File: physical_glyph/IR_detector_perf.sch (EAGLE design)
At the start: 18 parts, among them IC1 7805T, T1 BP103, U1 MCP6004-I/P, U2 LM339PWR

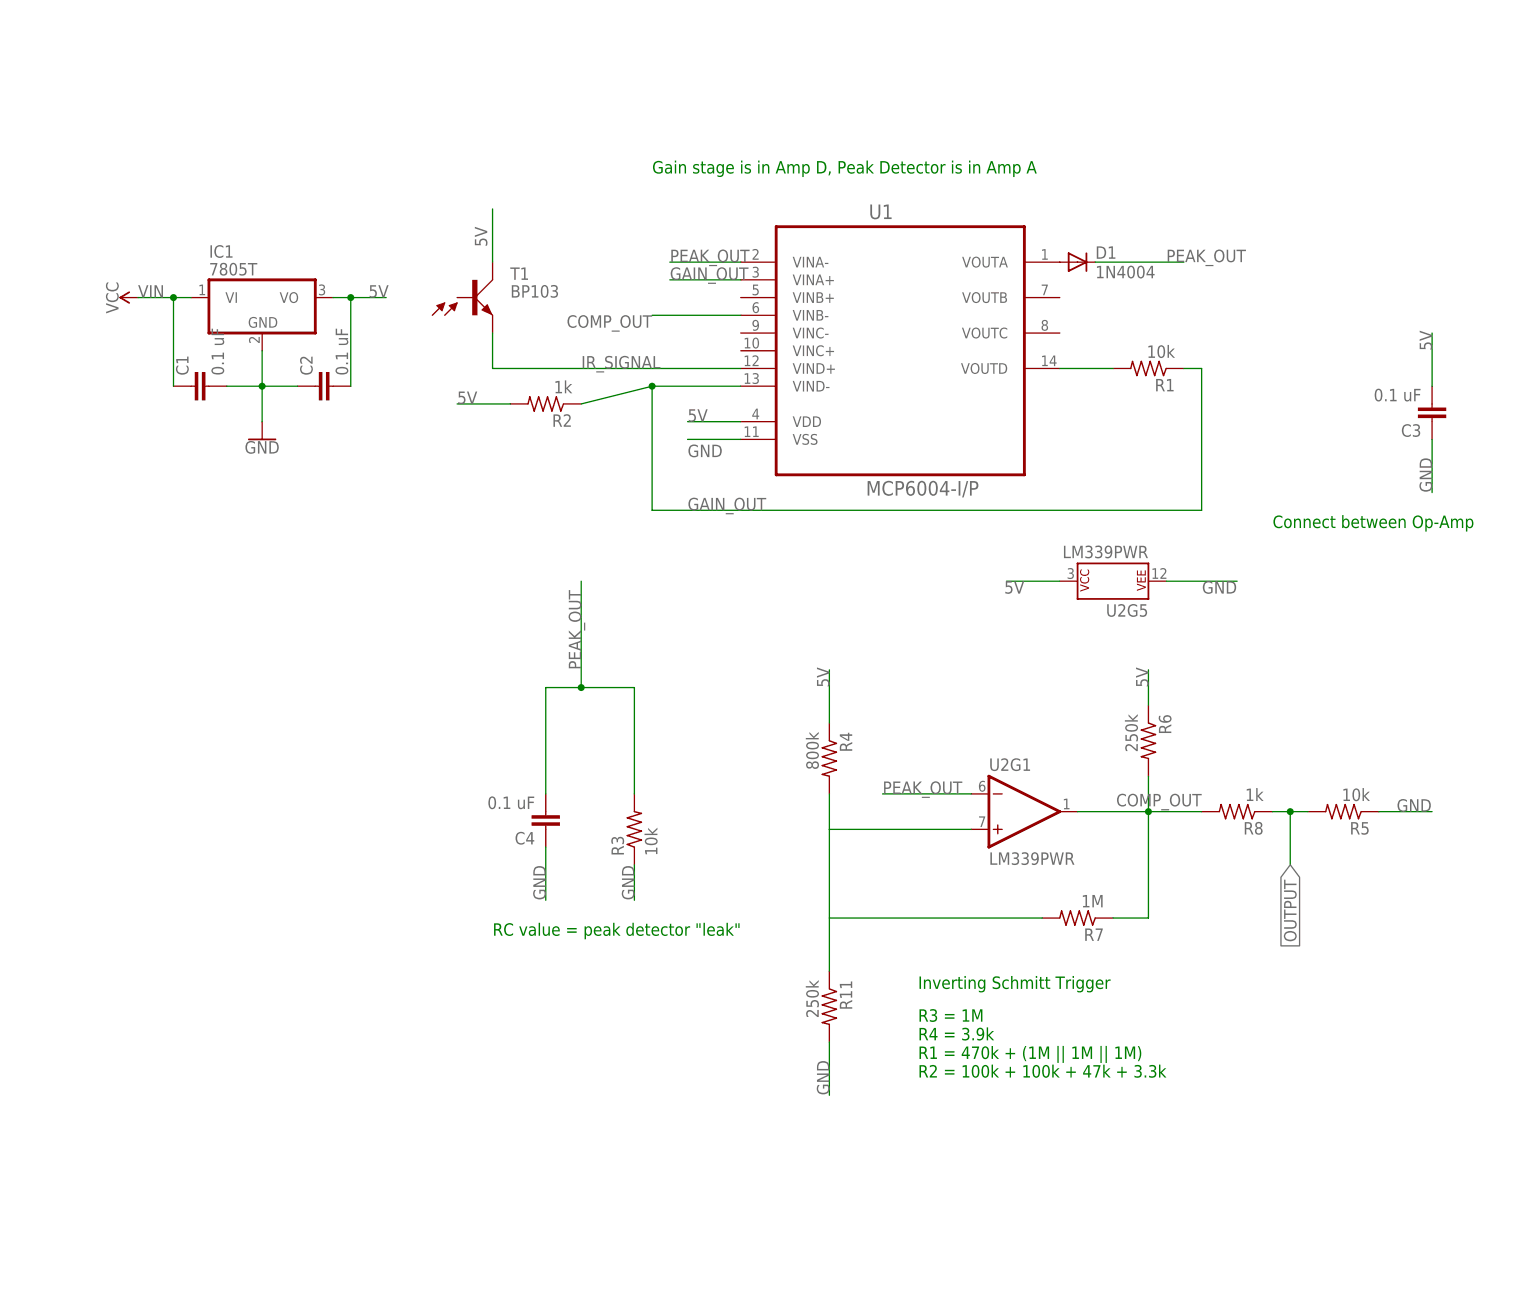
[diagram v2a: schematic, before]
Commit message: Change gain stage and output
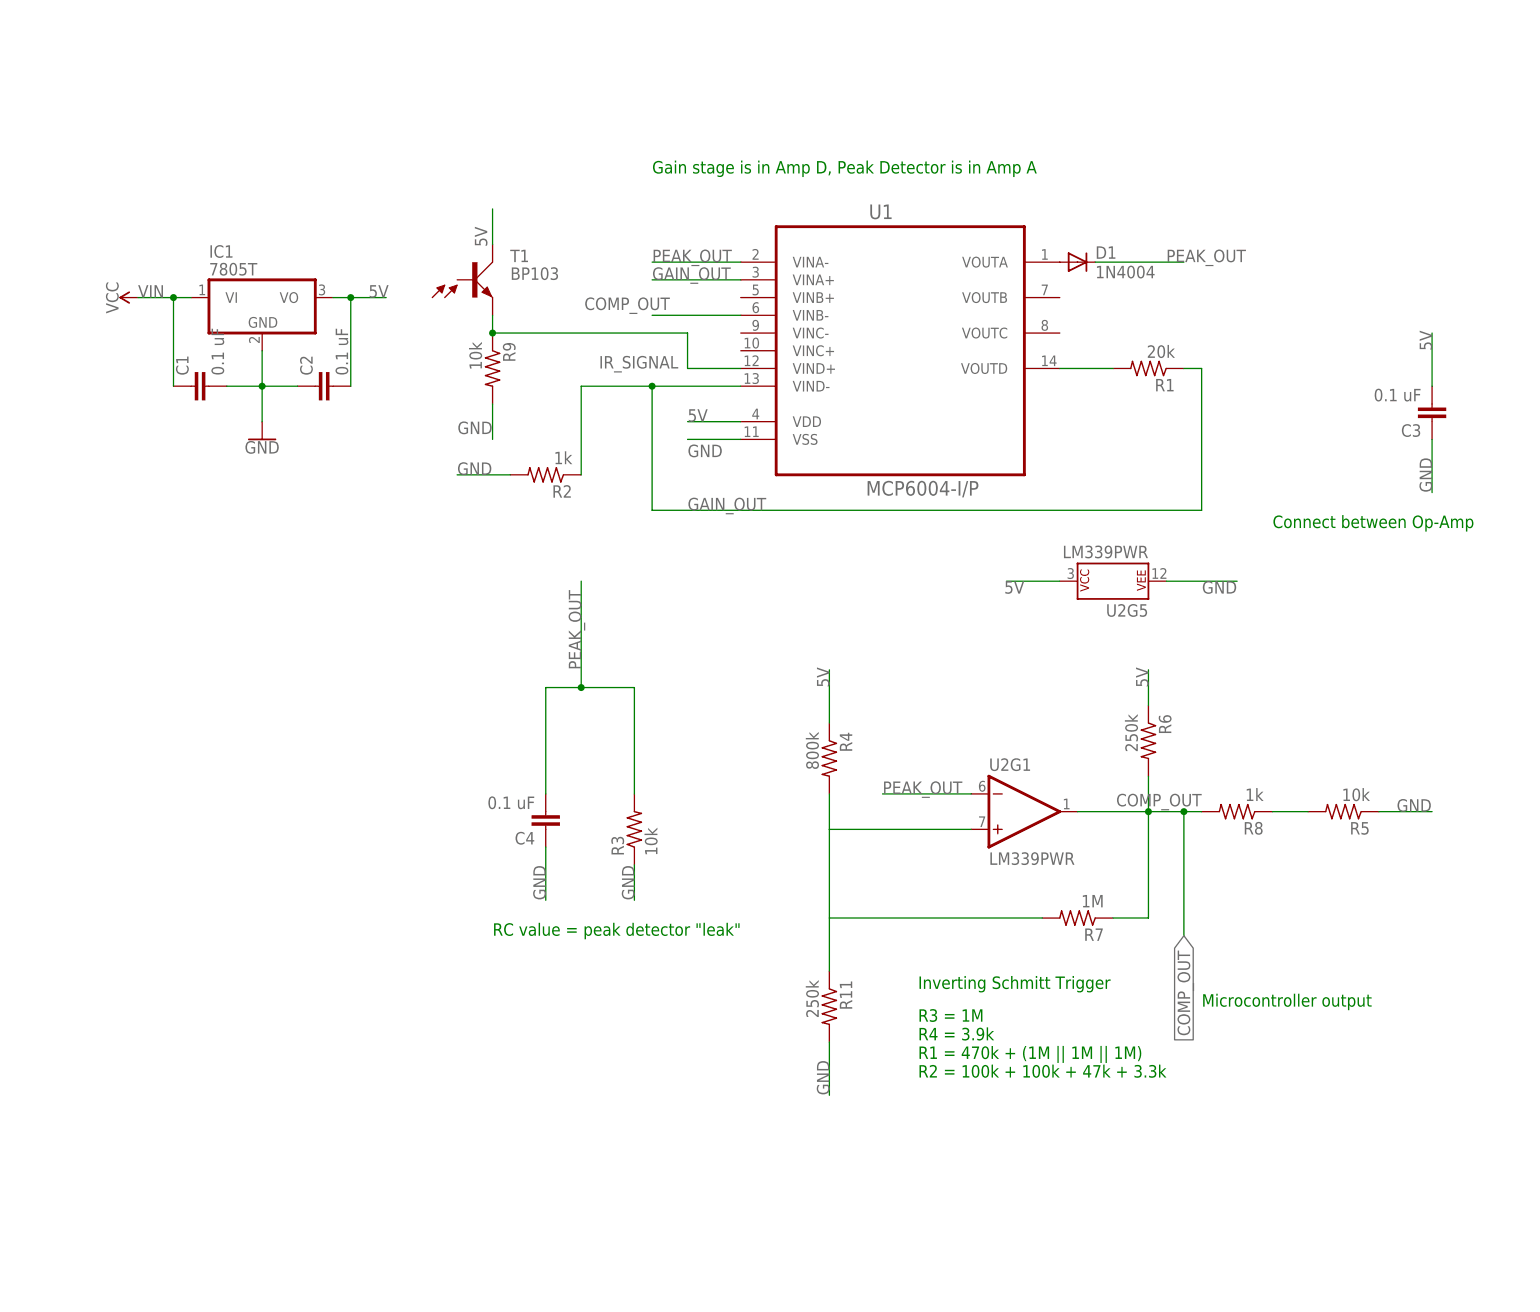
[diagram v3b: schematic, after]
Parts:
- added R9: 10k, rcl:R-US_0204/2V
- R1: value 10k -> 20k
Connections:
- net OUTPUT renamed N$1
- net 5V: no longer R2.2
- net GND: now also R2.2, R9.2
- net IR_SIGNAL: now also R9.1
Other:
- note added: "Microcontroller output"
- moved on the sheet: R2, T1
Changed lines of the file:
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@@
 <part name="C2" library="resistor" library_urn="urn:adsk.eagle:library:348" deviceset="C-EU" device="025-024X044" package3d_urn="urn:adsk.eagle:package:26149/1" value="0.1 uF"/>
 <part name="T1" library="opto-trans-siemens" library_urn="urn:adsk.eagle:library:317" deviceset="BP103" device="" package3d_urn="urn:adsk.eagle:package:21787/1"/>
-<part name="R1" library="rcl" library_urn="urn:adsk.eagle:library:334" deviceset="R-US_" device="0204/2V" package3d_urn="urn:adsk.eagle:package:23495/1" value="10k"/>
+<part name="R1" library="rcl" library_urn="urn:adsk.eagle:library:334" deviceset="R-US_" device="0204/2V" package3d_urn="urn:adsk.eagle:package:23495/1" value="20k"/>
 <part name="R2" library="rcl" library_urn="urn:adsk.eagle:library:334" deviceset="R-US_" device="0204/2V" package3d_urn="urn:adsk.eagle:package:23495/1" value="1k"/>
 <part name="R3" library="rcl" library_urn="urn:adsk.eagle:library:334" deviceset="R-US_" device="0204/2V" package3d_urn="urn:adsk.eagle:package:23495/1" value="10k"/>
@@
 <part name="R5" library="rcl" library_urn="urn:adsk.eagle:library:334" deviceset="R-US_" device="0204/2V" package3d_urn="urn:adsk.eagle:package:23495/1" value="10k"/>
 <part name="R8" library="rcl" library_urn="urn:adsk.eagle:library:334" deviceset="R-US_" device="0204/2V" package3d_urn="urn:adsk.eagle:package:23495/1" value="1k"/>
+<part name="R9" library="rcl" library_urn="urn:adsk.eagle:library:334" deviceset="R-US_" device="0204/2V" package3d_urn="urn:adsk.eagle:package:23495/1" value="10k"/>
 </parts>
 <sheets>
@@
 <text x="17.78" y="-7.62" size="1.778" layer="91">RC value = peak detector "leak"</text>
 <text x="78.74" y="-15.24" size="1.778" layer="91">Inverting Schmitt Trigger</text>
+<text x="119.38" y="-17.78" size="1.778" layer="91">Microcontroller output</text>
 </plain>
 <instances>
@@
 <instance part="C1" gate="G$1" x="-25.4" y="71.12" rot="R90"/>
 <instance part="C2" gate="G$1" x="-7.62" y="71.12" rot="R90"/>
-<instance part="T1" gate="1" x="15.24" y="83.82"/>
+<instance part="T1" gate="1" x="15.24" y="86.36"/>
 <instance part="R1" gate="G$1" x="111.76" y="73.66" rot="R180"/>
-<instance part="R2" gate="G$1" x="25.4" y="68.58" rot="R180"/>
+<instance part="R2" gate="G$1" x="25.4" y="58.42" rot="R180"/>
 <instance part="R3" gate="G$1" x="38.1" y="7.62" rot="R90"/>
 <instance part="R4" gate="G$1" x="66.04" y="17.78" rot="R270"/>
@@
 <instance part="R5" gate="G$1" x="139.7" y="10.16" rot="R180"/>
 <instance part="R8" gate="G$1" x="124.46" y="10.16" rot="R180"/>
+<instance part="R9" gate="G$1" x="17.78" y="73.66" rot="R270"/>
 </instances>
 <busses>
@@
 <segment>
 <pinref part="T1" gate="1" pin="C"/>
-<wire x1="17.78" y1="88.9" x2="17.78" y2="96.52" width="0.1524" layer="91"/>
+<wire x1="17.78" y1="91.44" x2="17.78" y2="96.52" width="0.1524" layer="91"/>
 <label x="15.24" y="93.98" size="1.778" layer="95" rot="R270"/>
-</segment>
-<segment>
-<pinref part="R2" gate="G$1" pin="2"/>
-<wire x1="20.32" y1="68.58" x2="12.7" y2="68.58" width="0.1524" layer="91"/>
-<label x="12.7" y="68.58" size="1.778" layer="95"/>
 </segment>
 <segment>
@@
 <label x="147.32" y="10.16" size="1.778" layer="95"/>
 </segment>
+<segment>
+<pinref part="R9" gate="G$1" pin="2"/>
+<wire x1="17.78" y1="68.58" x2="17.78" y2="63.5" width="0.1524" layer="91"/>
+<label x="17.78" y="66.04" size="1.778" layer="95" rot="R180"/>
+</segment>
+<segment>
+<pinref part="R2" gate="G$1" pin="2"/>
+<wire x1="20.32" y1="58.42" x2="12.7" y2="58.42" width="0.1524" layer="91"/>
+<label x="12.7" y="58.42" size="1.778" layer="95"/>
+</segment>
 </net>
 <net name="IR_SIGNAL" class="0">
 <segment>
 <pinref part="T1" gate="1" pin="E"/>
-<wire x1="17.78" y1="78.74" x2="17.78" y2="73.66" width="0.1524" layer="91"/>
+<wire x1="17.78" y1="81.28" x2="17.78" y2="78.74" width="0.1524" layer="91"/>
 <pinref part="U1" gate="A" pin="VIND+"/>
-<wire x1="17.78" y1="73.66" x2="53.34" y2="73.66" width="0.1524" layer="91"/>
-<label x="30.48" y="73.66" size="1.778" layer="95"/>
+<wire x1="17.78" y1="78.74" x2="45.72" y2="78.74" width="0.1524" layer="91"/>
+<wire x1="45.72" y1="78.74" x2="45.72" y2="73.66" width="0.1524" layer="91"/>
+<wire x1="45.72" y1="73.66" x2="53.34" y2="73.66" width="0.1524" layer="91"/>
+<label x="33.02" y="73.66" size="1.778" layer="95"/>
+<pinref part="R9" gate="G$1" pin="1"/>
+<junction x="17.78" y="78.74"/>
 </segment>
 </net>
@@
 <wire x1="40.64" y1="53.34" x2="40.64" y2="71.12" width="0.1524" layer="91"/>
 <pinref part="R2" gate="G$1" pin="1"/>
-<wire x1="30.48" y1="68.58" x2="40.64" y2="71.12" width="0.1524" layer="91"/>
+<wire x1="30.48" y1="58.42" x2="30.48" y2="71.12" width="0.1524" layer="91"/>
+<wire x1="30.48" y1="71.12" x2="40.64" y2="71.12" width="0.1524" layer="91"/>
 <junction x="40.64" y="71.12"/>
 <label x="45.72" y="53.34" size="1.778" layer="95"/>
@@
 <segment>
 <pinref part="U1" gate="A" pin="VINA+"/>
-<wire x1="53.34" y1="86.36" x2="43.18" y2="86.36" width="0.1524" layer="91"/>
-<label x="43.18" y="86.36" size="1.778" layer="95"/>
+<wire x1="53.34" y1="86.36" x2="40.64" y2="86.36" width="0.1524" layer="91"/>
+<label x="40.64" y="86.36" size="1.778" layer="95"/>
 </segment>
 </net>
@@
 <pinref part="U1" gate="A" pin="VINB-"/>
 <wire x1="53.34" y1="81.28" x2="40.64" y2="81.28" width="0.1524" layer="91"/>
-<label x="40.64" y="81.28" size="1.778" layer="95" rot="R180"/>
-</segment>
-<segment>
+<label x="43.18" y="83.82" size="1.778" layer="95" rot="R180"/>
+</segment>
+<segment>
+<label x="116.84" y="-7.62" size="1.778" layer="95" rot="R270" xref="yes"/>
+<wire x1="116.84" y1="10.16" x2="116.84" y2="-7.62" width="0.1524" layer="91"/>
 <pinref part="U2" gate="G1" pin="OUT"/>
 <label x="119.38" y="12.7" size="1.778" layer="95" rot="R180"/>
 <wire x1="101.6" y1="10.16" x2="111.76" y2="10.16" width="0.1524" layer="91"/>
 <pinref part="R7" gate="G$1" pin="1"/>
-<wire x1="111.76" y1="10.16" x2="119.38" y2="10.16" width="0.1524" layer="91"/>
+<wire x1="111.76" y1="10.16" x2="116.84" y2="10.16" width="0.1524" layer="91"/>
+<wire x1="116.84" y1="10.16" x2="119.38" y2="10.16" width="0.1524" layer="91"/>
 <wire x1="106.68" y1="-5.08" x2="111.76" y2="-5.08" width="0.1524" layer="91"/>
 <wire x1="111.76" y1="-5.08" x2="111.76" y2="10.16" width="0.1524" layer="91"/>
@@
 <wire x1="111.76" y1="15.24" x2="111.76" y2="10.16" width="0.1524" layer="91"/>
 <pinref part="R8" gate="G$1" pin="2"/>
-</segment>
-</net>
-<net name="OUTPUT" class="0">
-<segment>
-<label x="132.08" y="2.54" size="1.778" layer="95" rot="R270" xref="yes"/>
-<wire x1="132.08" y1="10.16" x2="132.08" y2="2.54" width="0.1524" layer="91"/>
-<pinref part="R8" gate="G$1" pin="1"/>
-<wire x1="129.54" y1="10.16" x2="132.08" y2="10.16" width="0.1524" layer="91"/>
-<pinref part="R5" gate="G$1" pin="2"/>
-<wire x1="132.08" y1="10.16" x2="134.62" y2="10.16" width="0.1524" layer="91"/>
-<junction x="132.08" y="10.16"/>
+<junction x="116.84" y="10.16"/>
 </segment>
 </net>
@@
 <segment>
 <pinref part="U1" gate="A" pin="VINA-"/>
-<wire x1="53.34" y1="88.9" x2="43.18" y2="88.9" width="0.1524" layer="91"/>
-<label x="43.18" y="88.9" size="1.778" layer="95"/>
+<wire x1="53.34" y1="88.9" x2="40.64" y2="88.9" width="0.1524" layer="91"/>
+<label x="40.64" y="88.9" size="1.778" layer="95"/>
 </segment>
 <segment>
@@
 </segment>
 </net>
+<net name="N$1" class="0">
+<segment>
+<pinref part="R8" gate="G$1" pin="1"/>
+<pinref part="R5" gate="G$1" pin="2"/>
+<wire x1="129.54" y1="10.16" x2="134.62" y2="10.16" width="0.1524" layer="91"/>
+</segment>
+</net>
